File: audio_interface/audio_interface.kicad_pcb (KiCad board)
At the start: 2 copper layers, 139.7 x 81.3 mm, 153 parts, among them J1 XLR3, J10 MIC_EXT, J11 INST_EXT, J12 Conn_01x01, J13 Test Headers, J14 SWD, J15 PCM_Jumper, J16 USB_B, J2 AudioJack2, J3 EXT_9V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

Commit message: Orion's layout
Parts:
- removed C26: 22u, Capacitor_SMD:CP_Elec_6.3x5.2
- removed J12: Conn_01x01, Connector_PinHeader_2.54mm:PinHeader_1x01_P2.54mm_Vertical
- added C8: 22u, Capacitor_SMD:CP_Elec_6.3x5.2, F.Cu at (233.4, 93.6)
- D7, D8: footprint LED_SMD:LED_1206_3216Metric_Pad1.42x1.75mm_HandSolder -> LED_THT:LED_D3.0mm
- J15: moved to F.Cu
- TP6: value M_BIAS -> I_BIAS
- TP7: value I_BIAS -> M_BIAS
- U1, U2, U3, U4: value NE5532 -> OPA2134
- moved C31 235.0 mm to (248.9, 109.5), turned to 90 degrees
- moved F1 231.6 mm to (259.1, 144.8), turned to 180 degrees
- moved C22 227.1 mm to (251.2, 86.4), turned to 180 degrees
- moved L2 223.5 mm to (238.5, 85.7), turned to 90 degrees
- moved R4 222.9 mm to (208.3, 144.8), turned to 90 degrees
- moved R19 222.4 mm to (252.7, 144.8), turned to -90 degrees
- moved JP10 222.1 mm to (255.3, 100.3), turned to 90 degrees
- moved C24 219.3 mm to (242.0, 90.8), turned to 180 degrees
- moved D1 215.9 mm to (250.2, 144.8), turned to -90 degrees
- moved C34 210.5 mm to (219.7, 113.0)
- moved R11 205.3 mm to (191.8, 118.1), turned to 180 degrees
- moved JP14 203.5 mm to (248.9, 118.1)
- moved C35 198.2 mm to (219.7, 105.4)
- moved C10 197.7 mm to (224.8, 144.8), turned to 90 degrees
- moved U1 197.7 mm to (222.2, 138.4), turned to -90 degrees
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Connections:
- C15 pad 1: VCOM_L -> VCOM_R
- C16 pad 1: VCOM_R -> VCOM_L
- JP7 pad 2: 2V5A_M -> 2V5A_I
- JP8 pad 2: 2V5A_I -> 2V5A_M
- U1 pad 1: MIC_OUT -> unconnected-(U1-Pad1)
- U1 pad 2: Net-(C9-Pad1) -> GNDA
- U1 pad 3: Net-(R14-Pad2) -> GNDA
- U1 pad 5: GNDA -> Net-(C2-Pad1)
- U1 pad 6: GNDA -> Net-(C5-Pad2)
- U1 pad 7: unconnected-(U1-Pad7) -> Net-(C5-Pad1)
- U2 pad 5: Net-(C2-Pad1) -> Net-(JP4-Pad2)
- U2 pad 6: Net-(C5-Pad2) -> Net-(C6-Pad2)
- U2 pad 7: Net-(C5-Pad1) -> Net-(C6-Pad1)
- U3 pad 5: Net-(JP4-Pad2) -> VCOM_R
- U3 pad 6: Net-(C6-Pad2) -> Net-(JP7-Pad1)
- U3 pad 7: Net-(C6-Pad1) -> Net-(JP7-Pad1)
- U4 pad 1: Net-(JP7-Pad1) -> MIC_OUT
- U4 pad 2: Net-(JP7-Pad1) -> Net-(C9-Pad1)
- U4 pad 3: VCOM_L -> Net-(R14-Pad2)
- U4 pad 5: VCOM_R -> VCOM_L
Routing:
- net VSSA: track 0.00 -> 161.6 mm, vias 0 -> 1
- net +9V: track 0.00 -> 152.5 mm
- net VAA: track 0.00 -> 148.0 mm, vias 0 -> 1
- net /Digital/PCM_CLK: track 0.00 -> 86.0 mm
- net /Digital/I2S_WS: track 0.00 -> 82.1 mm
- net /Digital/I2S_CLK: track 0.00 -> 78.2 mm
- net /Digital/CLIP_L: track 0.00 -> 74.2 mm, vias 0 -> 1
- net /Digital/I2S_SD: track 0.00 -> 73.5 mm
- net /Digital/CLIP_R: track 0.00 -> 73.0 mm, vias 0 -> 1
- net /Digital/PCM_RST_n: track 0.00 -> 71.7 mm, vias 0 -> 1
- net +5VA: track 0.00 -> 66.3 mm, vias 0 -> 1
- net +3V3: track 0.00 -> 66.3 mm, vias 0 -> 1
- net USB_5V: track 0.00 -> 65.3 mm, vias 0 -> 2
- net /Digital/RST_n: track 0.00 -> 58.9 mm, vias 0 -> 2
- net VCOM_R: track 0.00 -> 56.2 mm, vias 0 -> 1
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- added copper zone on F.Cu, net GNDD

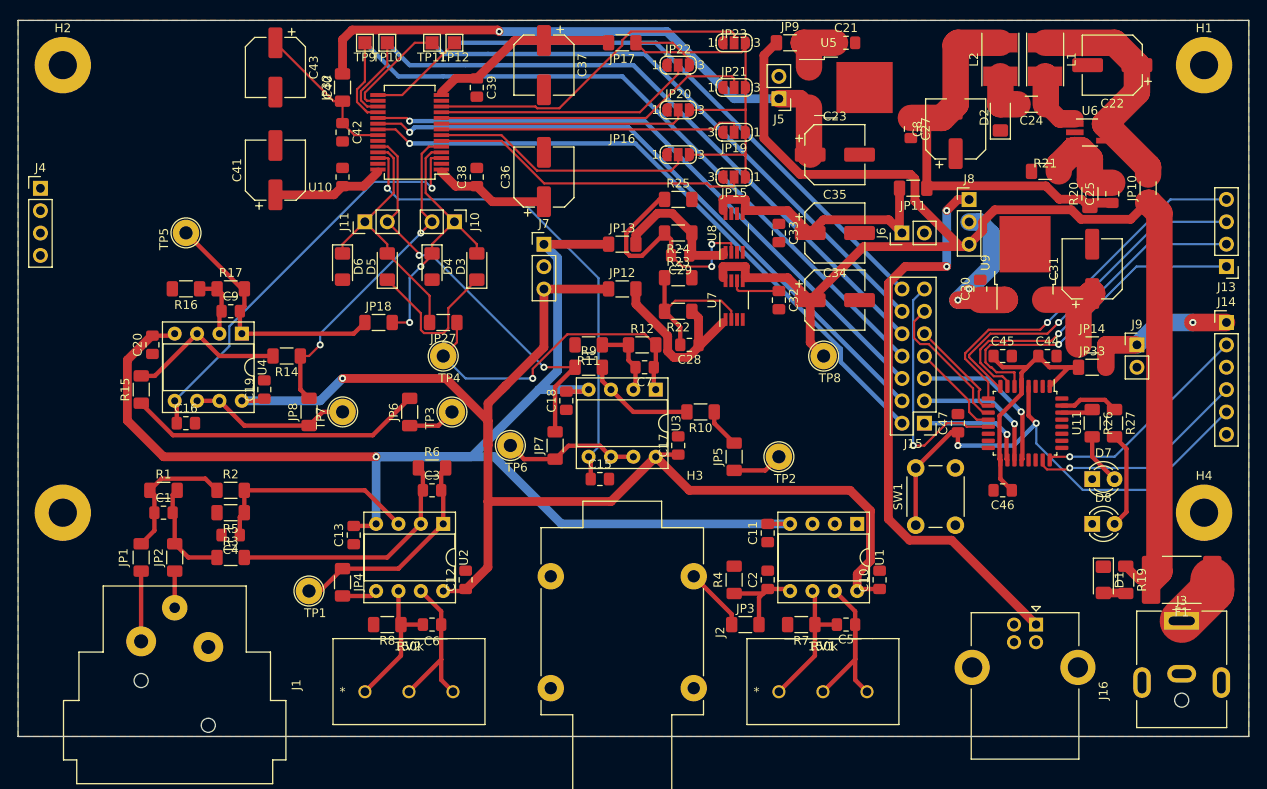
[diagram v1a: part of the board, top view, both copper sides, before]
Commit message: Fixed some layout issues. Flipped ADC.
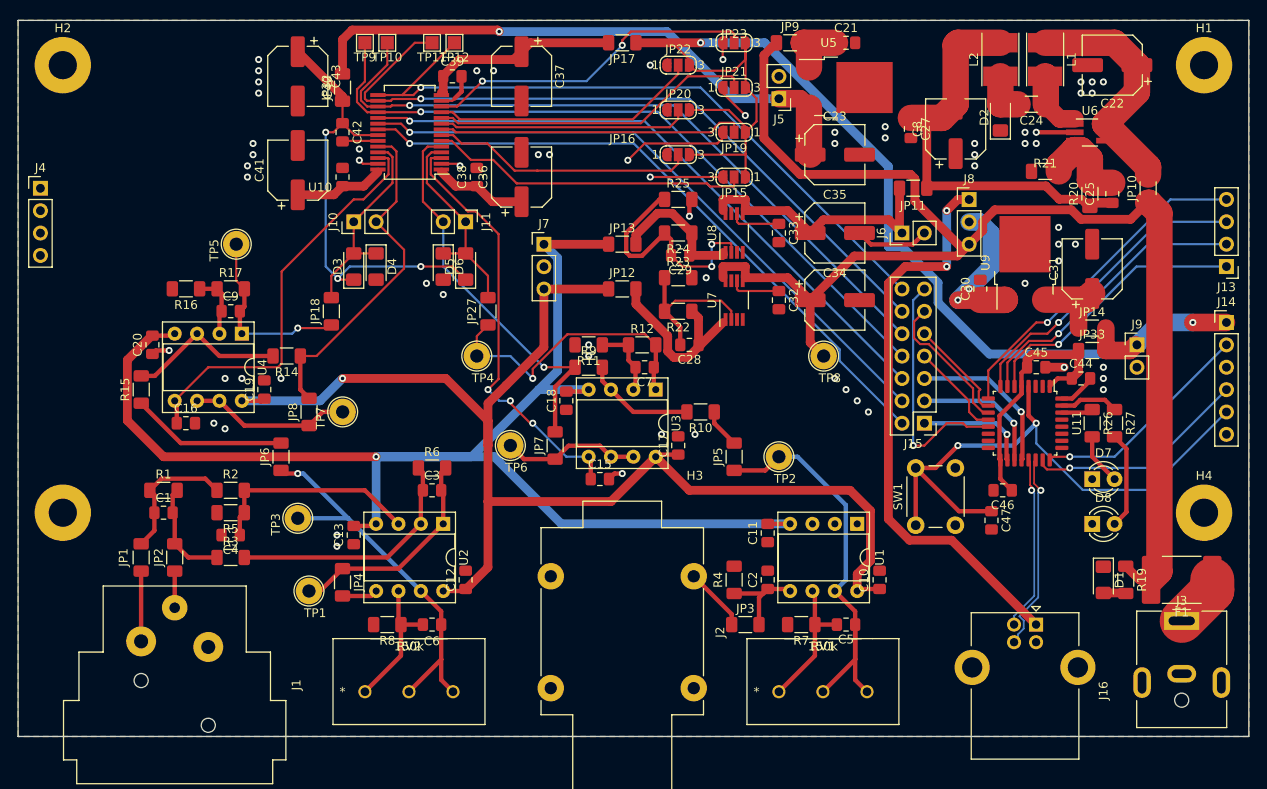
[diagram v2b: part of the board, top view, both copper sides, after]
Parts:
- moved TP3 21.3 mm to (158.8, 137.8)
- moved JP6 15.5 mm to (156.8, 130.8)
- moved D3 14.0 mm to (165.1, 109.2)
- moved C47 11.7 mm to (237.5, 138.0), turned to -90 degrees
- moved J10 11.4 mm to (165.1, 104.1), turned to 90 degrees
- moved J11 11.4 mm to (177.8, 104.1), turned to -90 degrees
- moved D6 11.4 mm to (175.3, 109.2)
- moved D5 8.89 mm to (177.8, 109.2)
- moved D4 6.35 mm to (167.6, 109.2)
- moved TP5 5.85 mm to (151.8, 106.7)
- moved JP18 5.51 mm to (162.6, 114.3), turned to 90 degrees
- moved JP27 5.24 mm to (180.3, 114.3), turned to 90 degrees
- moved C44 4.58 mm to (247.7, 121.9)
- moved C45 4.02 mm to (242.6, 120.7)
- moved TP4 3.81 mm to (179.1, 119.4)
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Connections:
- net /Digital/USB_DM renamed /Digital/USB_D_N
- net /Digital/USB_DP renamed /Digital/USB_D_P
- C15 pad 1: VCOM_R -> VCOM_L
- C16 pad 1: VCOM_L -> VCOM_R
- C21 pad 2: GNDD -> GNDA
- C22 pad 2: GNDD -> GNDA
- C27 pad 2: GNDD -> GNDA
- C30 pad 2: GNDD -> GNDA
- C31 pad 2: GNDD -> GNDA
- C37 pad 2: GNDD -> GNDA
- C39 pad 2: GNDD -> GNDA
- C42 pad 1: Net-(C42-Pad1) -> /Digital/ADC_5V
- C43 pad 1: Net-(C42-Pad1) -> /Digital/ADC_5V
- C44 pad 2: GNDD -> GNDA
- C45 pad 2: GNDD -> GNDA
- C46 pad 2: GNDD -> GNDA
- C47 pad 2: GNDD -> GNDA
- C8 pad 1: GNDD -> GNDA
- D1 pad 1: GNDD -> GNDA
- D2 pad 1: GNDD -> GNDA
- D3 pad 1: +5V -> /Digital/ADC_5V
- D5 pad 1: +5V -> /Digital/ADC_5V
- D7 pad 1: GNDD -> GNDA
- D8 pad 1: GNDD -> GNDA
- H1 pad 1: GNDD -> GNDA
- H2 pad 1: GNDD -> GNDA
- H3 pad 1: GNDD -> GNDA
- H4 pad 1: GNDD -> GNDA
- J16 pad 4: GNDD -> GNDA
- J16 pad 5: GNDD -> GNDA
- J3 pad 2: GNDD -> GNDA
- J4 pad 1: GNDD -> GNDA
- J4 pad 2: GNDD -> GNDA
- J4 pad 3: GNDD -> GNDA
- J4 pad 4: GNDD -> GNDA
- J5 pad 2: GNDD -> GNDA
- J6 pad 2: GNDD -> GNDA
- J9 pad 2: GNDD -> GNDA
- JP15 pad 3: GNDD -> GNDA
- JP16 pad 1: GNDD -> GNDA
- JP19 pad 3: GNDD -> GNDA
- JP20 pad 1: GNDD -> GNDA
- JP21 pad 1: GNDD -> GNDA
- JP22 pad 1: GNDD -> GNDA
- JP23 pad 1: GNDD -> GNDA
- JP32 pad 1: Net-(C42-Pad1) -> /Digital/ADC_5V
- R21 pad 2: GNDD -> GNDA
- SW1 pad 2: GNDD -> GNDA
- U10 pad 13: GNDD -> GNDA
- U10 pad 22: Net-(C42-Pad1) -> /Digital/ADC_5V
- U10 pad 24: 2V5A_I -> 2V5A_M
- U10 pad 25: /Digital/INST_ADC -> /Digital/MIC_ADC
- U10 pad 4: /Digital/MIC_ADC -> /Digital/INST_ADC
- U10 pad 5: 2V5A_M -> 2V5A_I
- U11 pad 16: GNDD -> GNDA
- U11 pad 32: GNDD -> GNDA
- U3 pad 5: VCOM_R -> VCOM_L
- U4 pad 5: VCOM_L -> VCOM_R
- U5 pad 2: GNDD -> GNDA
- U6 pad 2: GNDD -> GNDA
- U9 pad 2: GNDD -> GNDA
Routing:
- net +3V3: track 66.3 -> 142.9 mm, vias 1 -> 2
- net GNDA: track 0.00 -> 64.9 mm, vias 0 -> 66
- net /Digital/ADC_5V: track 0.00 -> 51.9 mm, vias 0 -> 3
- net /Digital/USB_D_P: track 0.00 -> 22.7 mm, vias 0 -> 1
- net Net-(C6-Pad1): track 23.6 -> 45.4 mm, vias 0 -> 1
- net Net-(C5-Pad1): track 27.8 -> 47.9 mm
- net /Digital/USB_D_N: track 0.00 -> 19.9 mm, vias 0 -> 1
- net +5V: track 17.6 -> 0.00 mm
- net Net-(C42-Pad1): track 17.4 -> 0.00 mm
- net Net-(JP6-Pad2): track 33.7 -> 17.8 mm
- net VCOM_R: track 56.2 -> 46.7 mm, vias 1 -> 0
- net /Digital/RST_n: track 58.9 -> 67.2 mm
- net MIC_OUT: track 29.2 -> 21.4 mm, vias 0 -> 1
- net /Digital/MIC_ADC: track 30.8 -> 23.3 mm, vias 2 -> 0
- net Net-(J13-Pad1): track 38.1 -> 31.4 mm
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- added copper zone on B.Cu, net GNDA
- added copper zone on F.Cu, net GNDA
- removed copper zone on F.Cu, net GNDD
